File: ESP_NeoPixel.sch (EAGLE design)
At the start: 2 parts

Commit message: did the thing
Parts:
- added C1, C3: 10µF, rcl:C-EUC0805
- added C2: 1nF, rcl:C-EUC0603
- added J3: MKDS3-2-5.00, jonas-phoenix:MKDS3-2-5.00
- added J4: MKDS3-3-5.00, jonas-phoenix:MKDS3-3-5.00
- added JP1: JUMPER-SMT_2_NO_SILK, SparkFun-Jumpers:JUMPER-SMT_2_NO_SILK
- added LOGO1: OSHW-LOGOS, SparkFun-Aesthetics:OSHW-LOGOS
- added Q1: BSN20,215, jonas_mosfet:BSN20,215
- added R1: 14.7k, rcl:R-EU_R0603
- added R2: 2.8k, rcl:R-EU_R0603
- added R3, R4: 4.7k, rcl:R-EU_R0603
- added U1: LMZ21700, jonas_ti:LMZ21700
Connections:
- removed net D5: J1.5
- new net N$1: R1.1, R2.2, U1.FB
- new net N$2: C2.1, U1.SS
- new net NEOPIX_3V3: J1.5, Q1.S, R3.1
- new net NEOPIX_5V: J4.2, Q1.D, R4.1
- new net VCC: C1.1, J3.1, J4.1, JP1.1, U1.EN, U1.VIN
- net +3V3: now also Q1.G, R3.2
- net +5V: now also C3.1, JP1.2, R1.2, R4.2, U1.VOS, U1.VOUT
- net GND: now also C1.2, C2.2, C3.2, J3.2, J4.3, R2.1, U1.GND

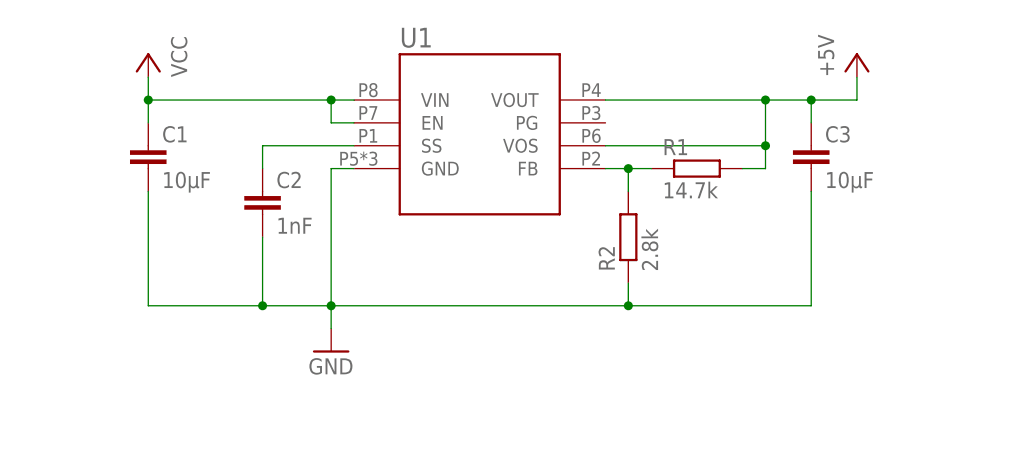
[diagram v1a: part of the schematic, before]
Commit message: values, silkscreen
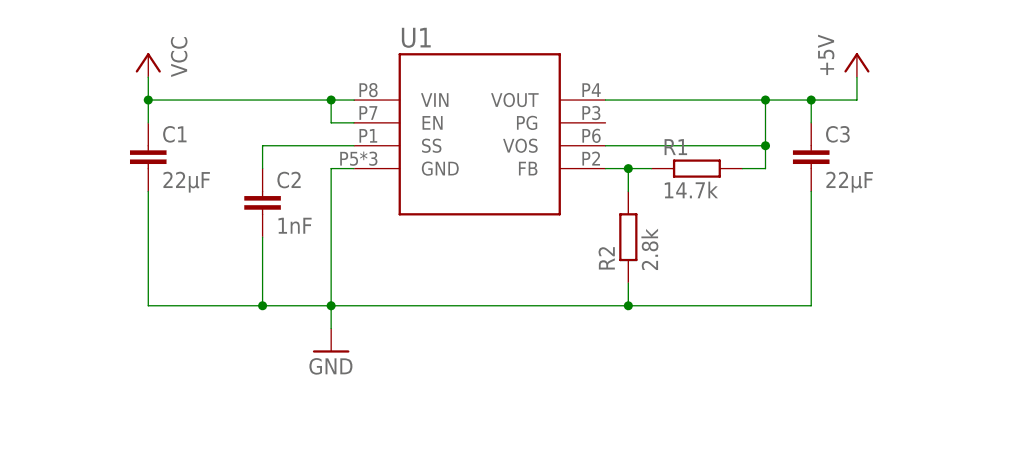
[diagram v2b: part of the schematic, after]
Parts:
- C1, C3: value 10µF -> 22µF
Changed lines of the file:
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@@
 <part name="U1" library="jonas_ti" library_urn="urn:adsk.eagle:library:539711" deviceset="LMZ21700" device=""/>
 <part name="GND4" library="supply1" library_urn="urn:adsk.eagle:library:371" deviceset="GND" device=""/>
-<part name="C3" library="rcl" library_urn="urn:adsk.eagle:library:334" deviceset="C-EU" device="C0805" package3d_urn="urn:adsk.eagle:package:23617/2" value="10µF"/>
+<part name="C3" library="rcl" library_urn="urn:adsk.eagle:library:334" deviceset="C-EU" device="C0805" package3d_urn="urn:adsk.eagle:package:23617/2" value="22µF"/>
 <part name="R1" library="rcl" library_urn="urn:adsk.eagle:library:334" deviceset="R-EU_" device="R0603" package3d_urn="urn:adsk.eagle:package:23555/2" value="14.7k"/>
 <part name="R2" library="rcl" library_urn="urn:adsk.eagle:library:334" deviceset="R-EU_" device="R0603" package3d_urn="urn:adsk.eagle:package:23555/2" value="2.8k"/>
 <part name="P+7" library="supply1" library_urn="urn:adsk.eagle:library:371" deviceset="VCC" device=""/>
 <part name="P+8" library="supply1" library_urn="urn:adsk.eagle:library:371" deviceset="+5V" device=""/>
-<part name="C1" library="rcl" library_urn="urn:adsk.eagle:library:334" deviceset="C-EU" device="C0805" package3d_urn="urn:adsk.eagle:package:23617/2" value="10µF"/>
+<part name="C1" library="rcl" library_urn="urn:adsk.eagle:library:334" deviceset="C-EU" device="C0805" package3d_urn="urn:adsk.eagle:package:23617/2" value="22µF"/>
 <part name="C2" library="rcl" library_urn="urn:adsk.eagle:library:334" deviceset="C-EU" device="C0603" package3d_urn="urn:adsk.eagle:package:23616/2" value="1nF"/>
 <part name="LOGO1" library="SparkFun-Aesthetics" library_urn="urn:adsk.eagle:library:507" deviceset="OSHW-LOGO" device="S" package3d_urn="urn:adsk.eagle:package:37099/1"/>

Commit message: leds
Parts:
- added LED1, LED2: (no value), led:LEDCHIP-LED0603
- added R5, R6: (no value), rcl:R-EU_R0603
- J1, J2: value (none) -> CONN_08; device SparkFun-Connectors:CONN_08LOCK_NO_SILK -> jonas_Sparkfun-Connectors:CONN_08
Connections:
- new net N$3: LED1.A, R5.1
- new net N$4: LED2.A, R6.1
- net D6: now also R5.2
- net D7: now also R6.2
- net GND: now also LED1.C, LED2.C
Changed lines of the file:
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@@
 </classes>
 <parts>
-<part name="J1" library="SparkFun-Connectors" library_urn="urn:adsk.eagle:library:513" deviceset="CONN_08" device="LOCK_NO_SILK" package3d_urn="urn:adsk.eagle:package:38147/1"/>
-<part name="J2" library="SparkFun-Connectors" library_urn="urn:adsk.eagle:library:513" deviceset="CONN_08" device="LOCK_NO_SILK" package3d_urn="urn:adsk.eagle:package:38147/1"/>
+<part name="J1" library="jonas_Sparkfun-Connectors" library_urn="urn:adsk.eagle:library:3855661" deviceset="CONN_08" device="" package3d_urn="urn:adsk.eagle:package:3855663/2"/>
+<part name="J2" library="jonas_Sparkfun-Connectors" library_urn="urn:adsk.eagle:library:3855661" deviceset="CONN_08" device="" package3d_urn="urn:adsk.eagle:package:3855663/2"/>
 <part name="+3V1" library="supply1" library_urn="urn:adsk.eagle:library:371" deviceset="+3V3" device=""/>
 <part name="P+1" library="supply1" library_urn="urn:adsk.eagle:library:371" deviceset="+5V" device=""/>
@@
 <part name="C2" library="rcl" library_urn="urn:adsk.eagle:library:334" deviceset="C-EU" device="C0603" package3d_urn="urn:adsk.eagle:package:23616/2" value="1nF"/>
 <part name="LOGO1" library="SparkFun-Aesthetics" library_urn="urn:adsk.eagle:library:507" deviceset="OSHW-LOGO" device="S" package3d_urn="urn:adsk.eagle:package:37099/1"/>
+<part name="LED1" library="led" library_urn="urn:adsk.eagle:library:259" deviceset="LED" device="CHIP-LED0603" package3d_urn="urn:adsk.eagle:package:15819/3"/>
+<part name="GND5" library="supply1" library_urn="urn:adsk.eagle:library:371" deviceset="GND" device=""/>
+<part name="R5" library="rcl" library_urn="urn:adsk.eagle:library:334" deviceset="R-EU_" device="R0603" package3d_urn="urn:adsk.eagle:package:23555/2"/>
+<part name="LED2" library="led" library_urn="urn:adsk.eagle:library:259" deviceset="LED" device="CHIP-LED0603" package3d_urn="urn:adsk.eagle:package:15819/3"/>
+<part name="GND6" library="supply1" library_urn="urn:adsk.eagle:library:371" deviceset="GND" device=""/>
+<part name="R6" library="rcl" library_urn="urn:adsk.eagle:library:334" deviceset="R-EU_" device="R0603" package3d_urn="urn:adsk.eagle:package:23555/2"/>
 </parts>
 <sheets>
@@
 </instance>
 <instance part="LOGO1" gate="G$1" x="213.36" y="78.74"/>
+<instance part="LED1" gate="G$1" x="38.1" y="142.24">
+<attribute name="NAME" x="41.656" y="137.668" size="1.778" layer="95" rot="R90"/>
+<attribute name="VALUE" x="43.815" y="137.668" size="1.778" layer="96" rot="R90"/>
+</instance>
+<instance part="GND5" gate="1" x="38.1" y="132.08">
+<attribute name="VALUE" x="35.56" y="129.54" size="1.778" layer="96"/>
+</instance>
+<instance part="R5" gate="G$1" x="38.1" y="152.4" rot="R90">
+<attribute name="NAME" x="36.6014" y="148.59" size="1.778" layer="95" rot="R90"/>
+<attribute name="VALUE" x="41.402" y="148.59" size="1.778" layer="96" rot="R90"/>
+</instance>
+<instance part="LED2" gate="G$1" x="45.72" y="142.24">
+<attribute name="VALUE" x="51.435" y="137.668" size="1.778" layer="96" rot="R90"/>
+</instance>
+<instance part="GND6" gate="1" x="45.72" y="132.08">
+<attribute name="VALUE" x="43.18" y="129.54" size="1.778" layer="96"/>
+</instance>
+<instance part="R6" gate="G$1" x="45.72" y="152.4" rot="R90">
+<attribute name="NAME" x="44.2214" y="148.59" size="1.778" layer="95" rot="R90"/>
+</instance>
 </instances>
 <busses>
@@
 <label x="35.56" y="35.56" size="1.778" layer="95"/>
 </segment>
+<segment>
+<pinref part="R5" gate="G$1" pin="2"/>
+<wire x1="38.1" y1="157.48" x2="38.1" y2="160.02" width="0.1524" layer="91"/>
+<label x="38.1" y="160.02" size="1.778" layer="95" rot="R90" xref="yes"/>
+</segment>
 </net>
 <net name="D7" class="0">
@@
 <wire x1="45.72" y1="33.02" x2="33.02" y2="33.02" width="0.1524" layer="91"/>
 <label x="35.56" y="33.02" size="1.778" layer="95"/>
+</segment>
+<segment>
+<pinref part="R6" gate="G$1" pin="2"/>
+<wire x1="45.72" y1="157.48" x2="45.72" y2="160.02" width="0.1524" layer="91"/>
+<label x="45.72" y="160.02" size="1.778" layer="95" rot="R90" xref="yes"/>
 </segment>
 </net>
@@
 <junction x="142.24" y="121.92"/>
 </segment>
+<segment>
+<pinref part="GND5" gate="1" pin="GND"/>
+<pinref part="LED1" gate="G$1" pin="C"/>
+<wire x1="38.1" y1="134.62" x2="38.1" y2="137.16" width="0.1524" layer="91"/>
+</segment>
+<segment>
+<pinref part="GND6" gate="1" pin="GND"/>
+<pinref part="LED2" gate="G$1" pin="C"/>
+<wire x1="45.72" y1="134.62" x2="45.72" y2="137.16" width="0.1524" layer="91"/>
+</segment>
 </net>
 <net name="+3V3" class="0">
@@
 </segment>
 </net>
+<net name="N$3" class="0">
+<segment>
+<pinref part="LED1" gate="G$1" pin="A"/>
+<pinref part="R5" gate="G$1" pin="1"/>
+<wire x1="38.1" y1="144.78" x2="38.1" y2="147.32" width="0.1524" layer="91"/>
+</segment>
+</net>
+<net name="N$4" class="0">
+<segment>
+<pinref part="LED2" gate="G$1" pin="A"/>
+<pinref part="R6" gate="G$1" pin="1"/>
+<wire x1="45.72" y1="144.78" x2="45.72" y2="147.32" width="0.1524" layer="91"/>
+</segment>
+</net>

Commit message: various layout changes
used sparkfun libraries
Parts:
- C1, C3: value 22µF -> 22uF; device rcl:C-EUC0805 -> SparkFun-Capacitors:22UF-0805-6.3V-20%
- C2: device rcl:C-EUC0603 -> SparkFun-Capacitors:1.0NF/1000PF-0603-50V-10%
- LED1, LED2: device led:LEDCHIP-LED0603 -> SparkFun-LED:LED0603
- LOGO1: value OSHW-LOGOS -> OSHW-LOGO; device SparkFun-Aesthetics:OSHW-LOGOS -> jonas_SparkFun-Aesthetics:OSHW-LOGO
- R1, R2: device rcl:R-EU_R0603 -> SparkFun-Resistors:RESISTOR0603
- R3, R4: device rcl:R-EU_R0603 -> SparkFun-Resistors:4.7KOHM-0603-1/10W-1%
- R5, R6: value (none) -> (none); device rcl:R-EU_R0603 -> SparkFun-Resistors:RESISTOR0603

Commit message: silkscreen fixes
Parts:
- LOGO1: value OSHW-LOGO -> OSHW-LOGOS; device jonas_SparkFun-Aesthetics:OSHW-LOGO -> SparkFun-Aesthetics:OSHW-LOGOS
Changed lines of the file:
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@@
 <part name="C1" library="SparkFun-Capacitors" library_urn="urn:adsk.eagle:library:510" deviceset="22UF" device="-0805-6.3V-20%" package3d_urn="urn:adsk.eagle:package:37429/1" value="22uF"/>
 <part name="C2" library="SparkFun-Capacitors" library_urn="urn:adsk.eagle:library:510" deviceset="1.0NF/1000PF" device="-0603-50V-10%" package3d_urn="urn:adsk.eagle:package:37414/1" value="1nF"/>
-<part name="LOGO1" library="jonas_SparkFun-Aesthetics" library_urn="urn:adsk.eagle:library:3855705" deviceset="OSHW-LOGO" device="" package3d_urn="urn:adsk.eagle:package:3855707/2"/>
+<part name="LOGO1" library="SparkFun-Aesthetics" library_urn="urn:adsk.eagle:library:507" deviceset="OSHW-LOGO" device="S" package3d_urn="urn:adsk.eagle:package:37099/1"/>
 <part name="LED1" library="SparkFun-LED" library_urn="urn:adsk.eagle:library:529" deviceset="LED" device="0603" package3d_urn="urn:adsk.eagle:package:39354/1"/>
 <part name="GND5" library="supply1" library_urn="urn:adsk.eagle:library:371" deviceset="GND" device=""/>
